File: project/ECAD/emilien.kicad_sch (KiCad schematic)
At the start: 11 parts, among them J1 Barrel_Jack_Switch, J2 Moteur 1, J3 Moteur 2, U1 ESP32-S3-UNO, U2 R-78E5.0-1.0

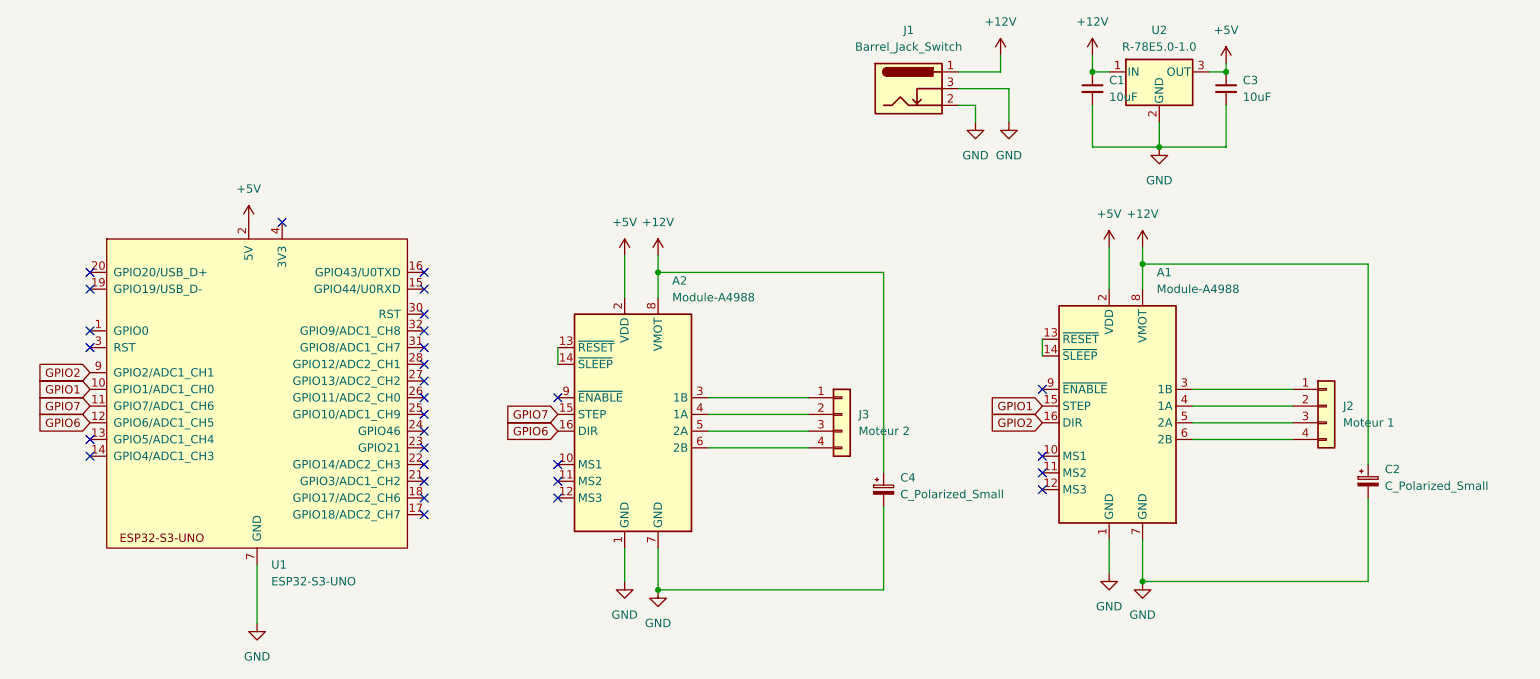
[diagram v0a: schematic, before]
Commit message: Kikad V2 modification d'alban effectué
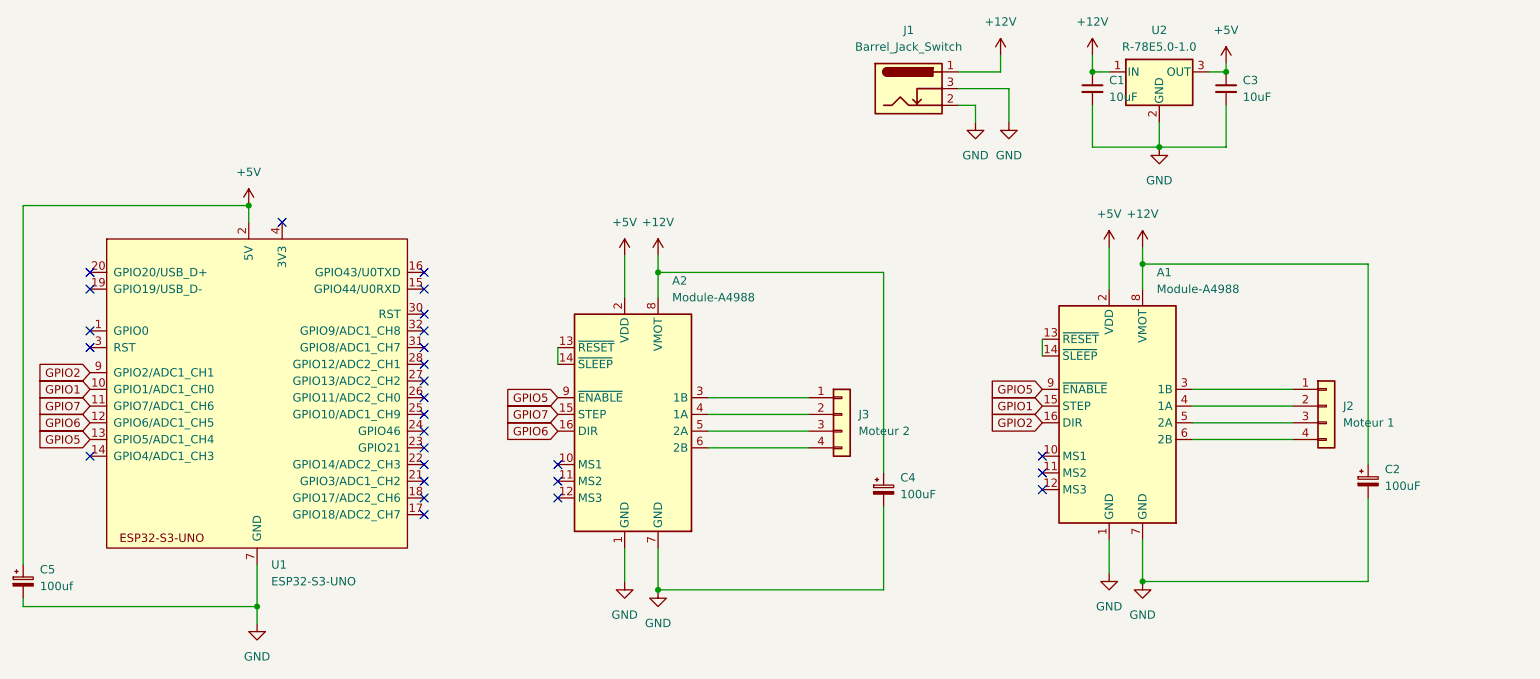
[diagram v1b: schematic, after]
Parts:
- added C5: 100uf, symbol Device:C_Polarized_Small
- C2, C4: value C_Polarized_Small -> 100uF
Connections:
- net +5V: now also C5.1
- net GND: now also C5.2
- net GPIO5: now reaches A2.9 (~{ENABLE})
- net GPIO5: now also A1.9 (~{ENABLE}), U1.13 (GPIO5/ADC1_CH4)
- no-connect marks 30 -> 27
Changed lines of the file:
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@@
+	)
+	(junction
+		(at 92.71 120.65)
+		(diameter 0)
+		(color 0 0 0 0)
 	)
 	(junction
@@
 	)
 	(junction
+		(at 91.44 59.69)
+		(diameter 0)
+		(color 0 0 0 0)
+	)
+	(junction
 		(at 229.87 50.8)
 		(diameter 0)
@@
 	)
 	(no_connect
-		(at 138.43 88.9)
-	)
-	(no_connect
 		(at 138.43 104.14)
 	)
@@
 	)
 	(no_connect
-		(at 212.09 87.63)
-	)
-	(no_connect
 		(at 138.43 101.6)
 	)
@@
 	)
 	(no_connect
-		(at 67.31 95.25)
-	)
-	(no_connect
 		(at 118.11 106.68)
 	)
@@
 	(wire
 		(pts
+			(xy 57.15 59.69) (xy 57.15 114.3)
+		)
+		(stroke
+			(width 0)
+			(type default)
+		)
+	)
+	(wire
+		(pts
 			(xy 161.29 93.98) (xy 176.53 93.98)
 		)
@@
 	(wire
 		(pts
+			(xy 57.15 120.65) (xy 92.71 120.65)
+		)
+		(stroke
+			(width 0)
+			(type default)
+		)
+	)
+	(wire
+		(pts
 			(xy 153.67 111.76) (xy 153.67 118.11)
 		)
@@
 	(wire
 		(pts
+			(xy 92.71 120.65) (xy 92.71 123.19)
+		)
+		(stroke
+			(width 0)
+			(type default)
+		)
+	)
+	(wire
+		(pts
 			(xy 227.33 68.58) (xy 227.33 66.04)
 		)
@@
 	(wire
 		(pts
+			(xy 91.44 59.69) (xy 91.44 62.23)
+		)
+		(stroke
+			(width 0)
+			(type default)
+		)
+	)
+	(wire
+		(pts
 			(xy 234.95 95.25) (xy 250.19 95.25)
 		)
@@
 	(wire
 		(pts
+			(xy 57.15 120.65) (xy 57.15 119.38)
+		)
+		(stroke
+			(width 0)
+			(type default)
+		)
+	)
+	(wire
+		(pts
 			(xy 205.74 36.83) (xy 205.74 39.37)
 		)
@@
 	(wire
 		(pts
-			(xy 92.71 114.3) (xy 92.71 123.19)
-		)
-		(stroke
-			(width 0)
-			(type default)
-		)
-	)
-	(wire
-		(pts
 			(xy 240.03 38.1) (xy 240.03 39.37)
 		)
@@
 	(wire
 		(pts
+			(xy 92.71 114.3) (xy 92.71 120.65)
+		)
+		(stroke
+			(width 0)
+			(type default)
+		)
+	)
+	(wire
+		(pts
 			(xy 161.29 88.9) (xy 176.53 88.9)
 		)
@@
 		(pts
 			(xy 234.95 87.63) (xy 250.19 87.63)
+		)
+		(stroke
+			(width 0)
+			(type default)
+		)
+	)
+	(wire
+		(pts
+			(xy 57.15 59.69) (xy 91.44 59.69)
 		)
 		(stroke
@@
 		)
 	)
+	(global_label "GPIO5"
+		(shape input)
+		(at 212.09 87.63 180)
+		(fields_autoplaced yes)
+		(effects
+			(font
+				(size 1.27 1.27)
+			)
+			(justify right)
+		)
+		(property "Intersheetrefs" "${INTERSHEET_REFS}"
+			(at 203.42 87.63 0)
+			(effects
+				(font
+					(size 1.27 1.27)
+				)
+				(justify right)
+				(hide yes)
+			)
+		)
+	)
+	(global_label "GPIO5"
+		(shape input)
+		(at 138.43 88.9 180)
+		(fields_autoplaced yes)
+		(effects
+			(font
+				(size 1.27 1.27)
+			)
+			(justify right)
+		)
+		(property "Intersheetrefs" "${INTERSHEET_REFS}"
+			(at 129.76 88.9 0)
+			(effects
+				(font
+					(size 1.27 1.27)
+				)
+				(justify right)
+				(hide yes)
+			)
+		)
+	)
 	(global_label "GPIO6"
 		(shape input)
@@
 		(property "Intersheetrefs" "${INTERSHEET_REFS}"
 			(at 58.64 92.71 0)
+			(effects
+				(font
+					(size 1.27 1.27)
+				)
+				(justify right)
+				(hide yes)
+			)
+		)
+	)
+	(global_label "GPIO5"
+		(shape input)
+		(at 67.31 95.25 180)
+		(fields_autoplaced yes)
+		(effects
+			(font
+				(size 1.27 1.27)
+			)
+			(justify right)
+		)
+		(property "Intersheetrefs" "${INTERSHEET_REFS}"
+			(at 58.64 95.25 0)
 			(effects
 				(font
@@
 			)
 		)
-		(property "Value" "C_Polarized_Small"
+		(property "Value" "100uF"
 			(at 264.16 102.3238 0)
 			(effects
@@
 			)
 		)
-		(property "Value" "C_Polarized_Small"
+		(property "Value" "100uF"
 			(at 190.5 103.5938 0)
 			(effects
@@
 	(symbol
 		(lib_id "power:+5V")
-		(at 91.44 62.23 0)
+		(at 91.44 59.69 0)
 		(unit 1)
 		(exclude_from_sim no)
@@
 		(fields_autoplaced yes)
 		(property "Reference" "#PWR02"
-			(at 91.44 66.04 0)
+			(at 91.44 63.5 0)
 			(effects
 				(font
@@
 		)
 		(property "Value" "+5V"
-			(at 91.44 57.15 0)
+			(at 91.44 54.61 0)
 			(effects
 				(font
@@
 		)
 		(property "Footprint" ""
-			(at 91.44 62.23 0)
+			(at 91.44 59.69 0)
 			(effects
 				(font
@@
 		)
 		(property "Datasheet" ""
-			(at 91.44 62.23 0)
+			(at 91.44 59.69 0)
 			(effects
 				(font
@@
 		)
 		(property "Description" "Power symbol creates a global label with name \"+5V\""
-			(at 91.44 62.23 0)
+			(at 91.44 59.69 0)
 			(effects
 				(font
@@
 					(unit 1)
 				)
+			)
+		)
+	)
+	(symbol
+		(lib_id "Device:C_Polarized_Small")
+		(at 57.15 116.84 0)
+		(unit 1)
+		(exclude_from_sim no)
+		(in_bom yes)
+		(on_board yes)
+		(dnp no)
+		(fields_autoplaced yes)
+		(property "Reference" "C5"
+			(at 59.69 115.0238 0)
+			(effects
+				(font
+					(size 1.27 1.27)
+				)
+				(justify left)
+			)
+		)
+		(property "Value" "100uf"
+			(at 59.69 117.5638 0)
+			(effects
+				(font
+					(size 1.27 1.27)
+				)
+				(justify left)
+			)
+		)
+		(property "Footprint" ""
+			(at 57.15 116.84 0)
+			(effects
+				(font
+					(size 1.27 1.27)
+				)
+				(hide yes)
+			)
+		)
+		(property "Datasheet" "~"
+			(at 57.15 116.84 0)
+			(effects
+				(font
+					(size 1.27 1.27)
+				)
+				(hide yes)
+			)
+		)
+		(property "Description" "Polarized capacitor, small symbol"
+			(at 57.15 116.84 0)
+			(effects
+				(font
+					(size 1.27 1.27)
+				)
+				(hide yes)
+			)
+		)
+		(pin "1"
+		)
+		(pin "2"
+		)
+		(instances
+			(project "emilien"
+				(path "/652b3968-8268-40f6-8bbe-d5819dbbe3de"
+					(reference "C5")
+					(unit 1)
+				)
